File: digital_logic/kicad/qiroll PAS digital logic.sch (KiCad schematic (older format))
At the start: 21 parts, among them U1 14538, U2 4023, U3 4027, U4 14538, U5 L7805

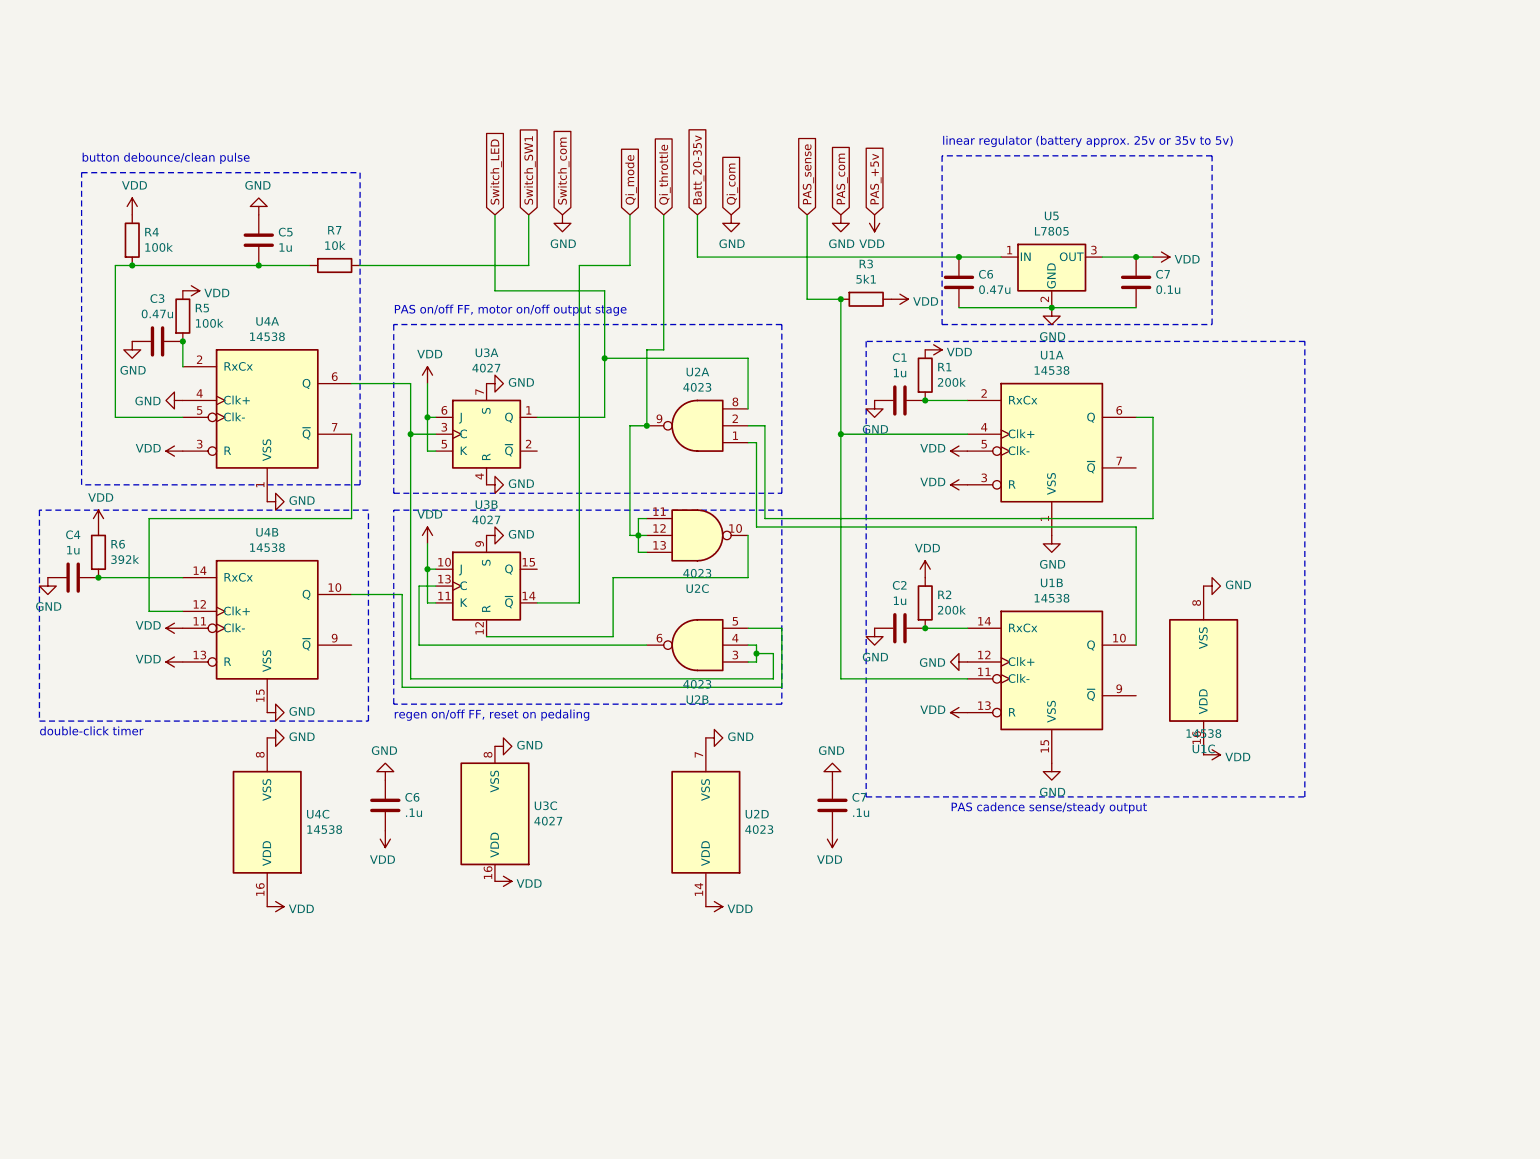
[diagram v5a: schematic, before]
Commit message: add electrolytic caps for stability
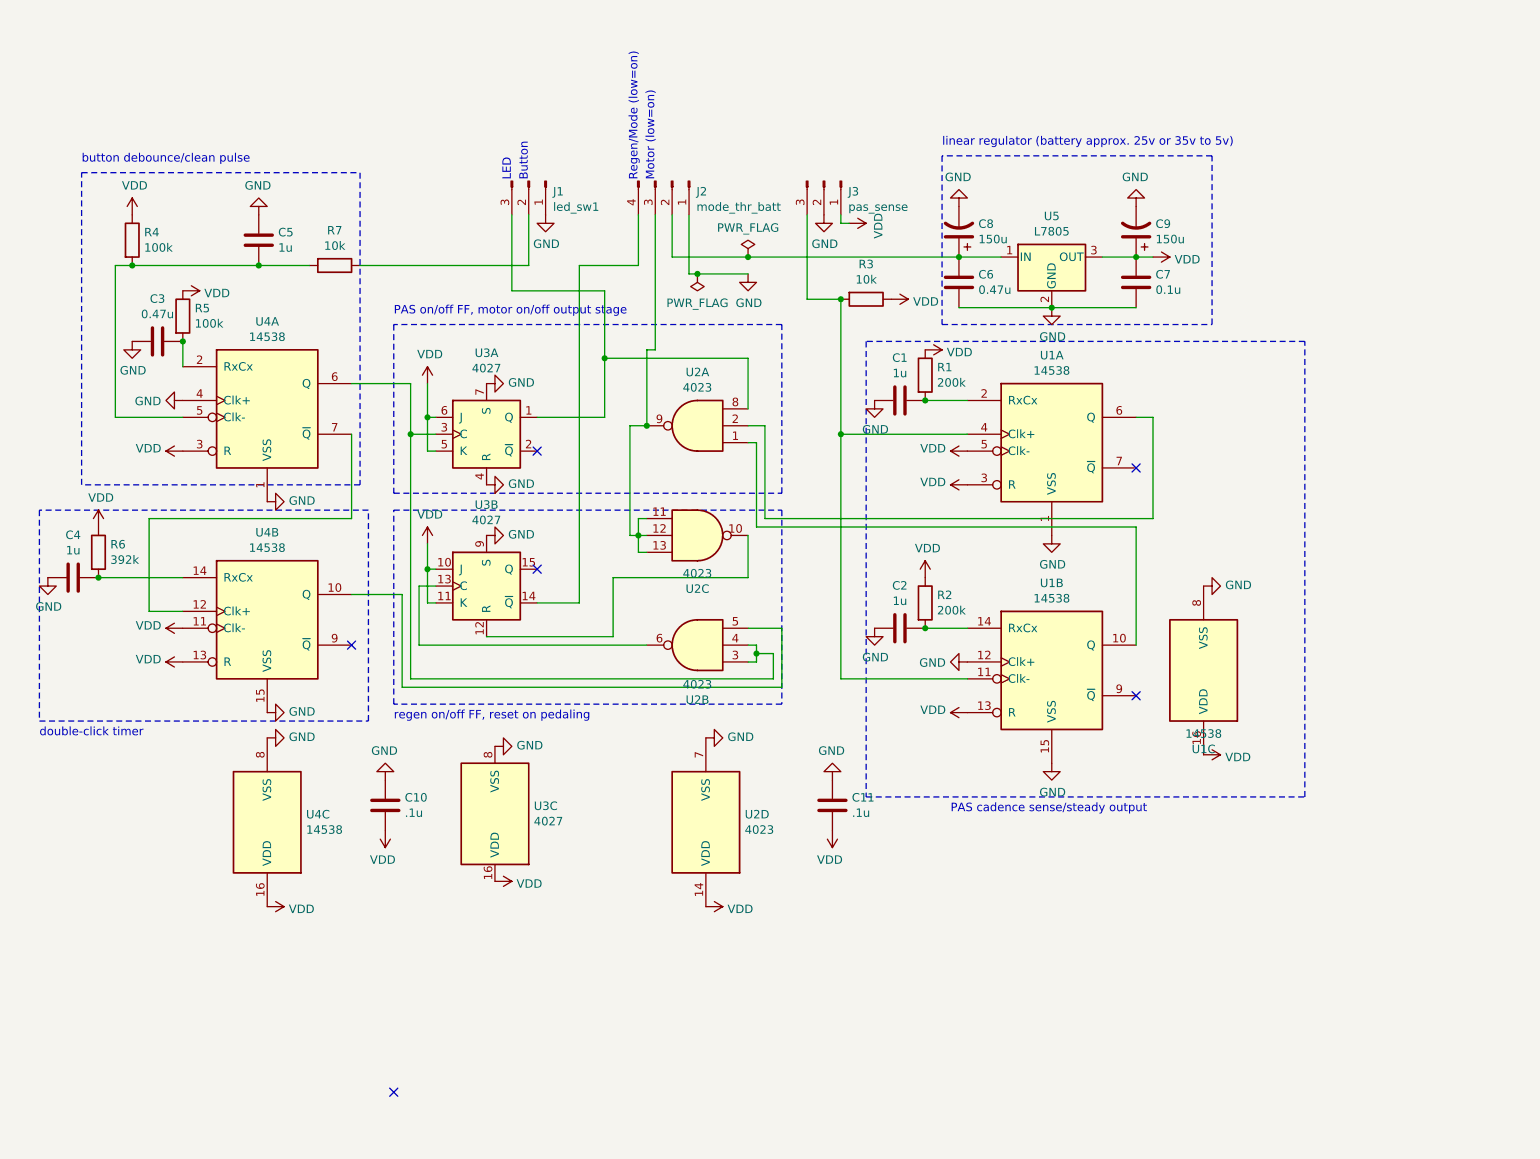
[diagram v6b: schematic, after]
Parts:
- added C8: 150u, Capacitor_THT:CP_Radial_D10.0mm_P5.00mm, symbol Device:CP1
- added C9: 150u, Capacitor_THT:CP_Radial_D5.0mm_P2.00mm, symbol Device:CP1
- added J1: led_sw1, Connector_PinHeader_2.54mm:PinHeader_1x03_P2.54mm_Vertical, symbol Connector:Conn_01x03_Male
- added J2: mode_thr_batt, Connector_Molex:Molex_KK-254_AE-6410-04A_1x04_P2.54mm_Vertical, symbol Connector:Conn_01x04_Male
- added J3: pas_sense, Connector_Molex:Molex_KK-254_AE-6410-03A_1x03_P2.54mm_Vertical, symbol Connector:Conn_01x03_Male
- C1, C2, C6, C7: footprint (none) -> Capacitor_SMD:C_0603_1608Metric
- C10: renamed from C6; footprint (none) -> Capacitor_SMD:C_0603_1608Metric
- C11: renamed from C7; footprint (none) -> Capacitor_SMD:C_0603_1608Metric
- C3, C4, C5: footprint (none) -> Capacitor_SMD:C_0201_0603Metric
- R1, R2, R4, R5, R6, R7: footprint (none) -> Resistor_SMD:R_0603_1608Metric
- R3: value 5k1 -> 10k; footprint (none) -> Resistor_SMD:R_0603_1608Metric
- U1, U3, U4: footprint (none) -> Package_SO:TSSOP-16_4.4x5mm_P0.65mm
- U2: footprint (none) -> Package_SO:TSSOP-14_4.4x5mm_P0.65mm
- U5: footprint (none) -> Package_TO_SOT_THT:TO-92
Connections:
- net GND: now also C8.2, C9.2, J1.1 (Pin_1), J2.1 (Pin_1), J3.2 (Pin_2)
- net VDD: now also C9.1, J3.1 (Pin_1)
- net Batt_20-35v: no longer names the net of C6.1, U5.1 (IN)
- net Batt_20-35v: now also C8.1, J2.2 (Pin_2)
- net PAS_sense: no longer names the net of R3.2, U1.11 (Clk-), U1.4 (Clk+)
- net PAS_sense: now also J3.3 (Pin_3)
- net Qi_mode: no longer names the net of U3.14 (~Q)
- net Qi_mode: now also J2.4 (Pin_4)
- net Qi_throttle: no longer names the net of U2.11, U2.12, U2.13, U2.9
- net Qi_throttle: now also J2.3 (Pin_3)
- net Switch_LED: no longer names the net of U2.8, U3.1 (Q)
- net Switch_LED: now also J1.3 (Pin_3)
- net Switch_SW1: no longer names the net of R7.1
- net Switch_SW1: now also J1.2 (Pin_2)
- no-connect marks 0 -> 6
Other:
- note added: "Button"
- note added: "LED"
- note added: "Motor (low=on)"
- note added: "Regen/Mode (low=on)"

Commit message: add voltage reg caps to schematic.png, start work on v2
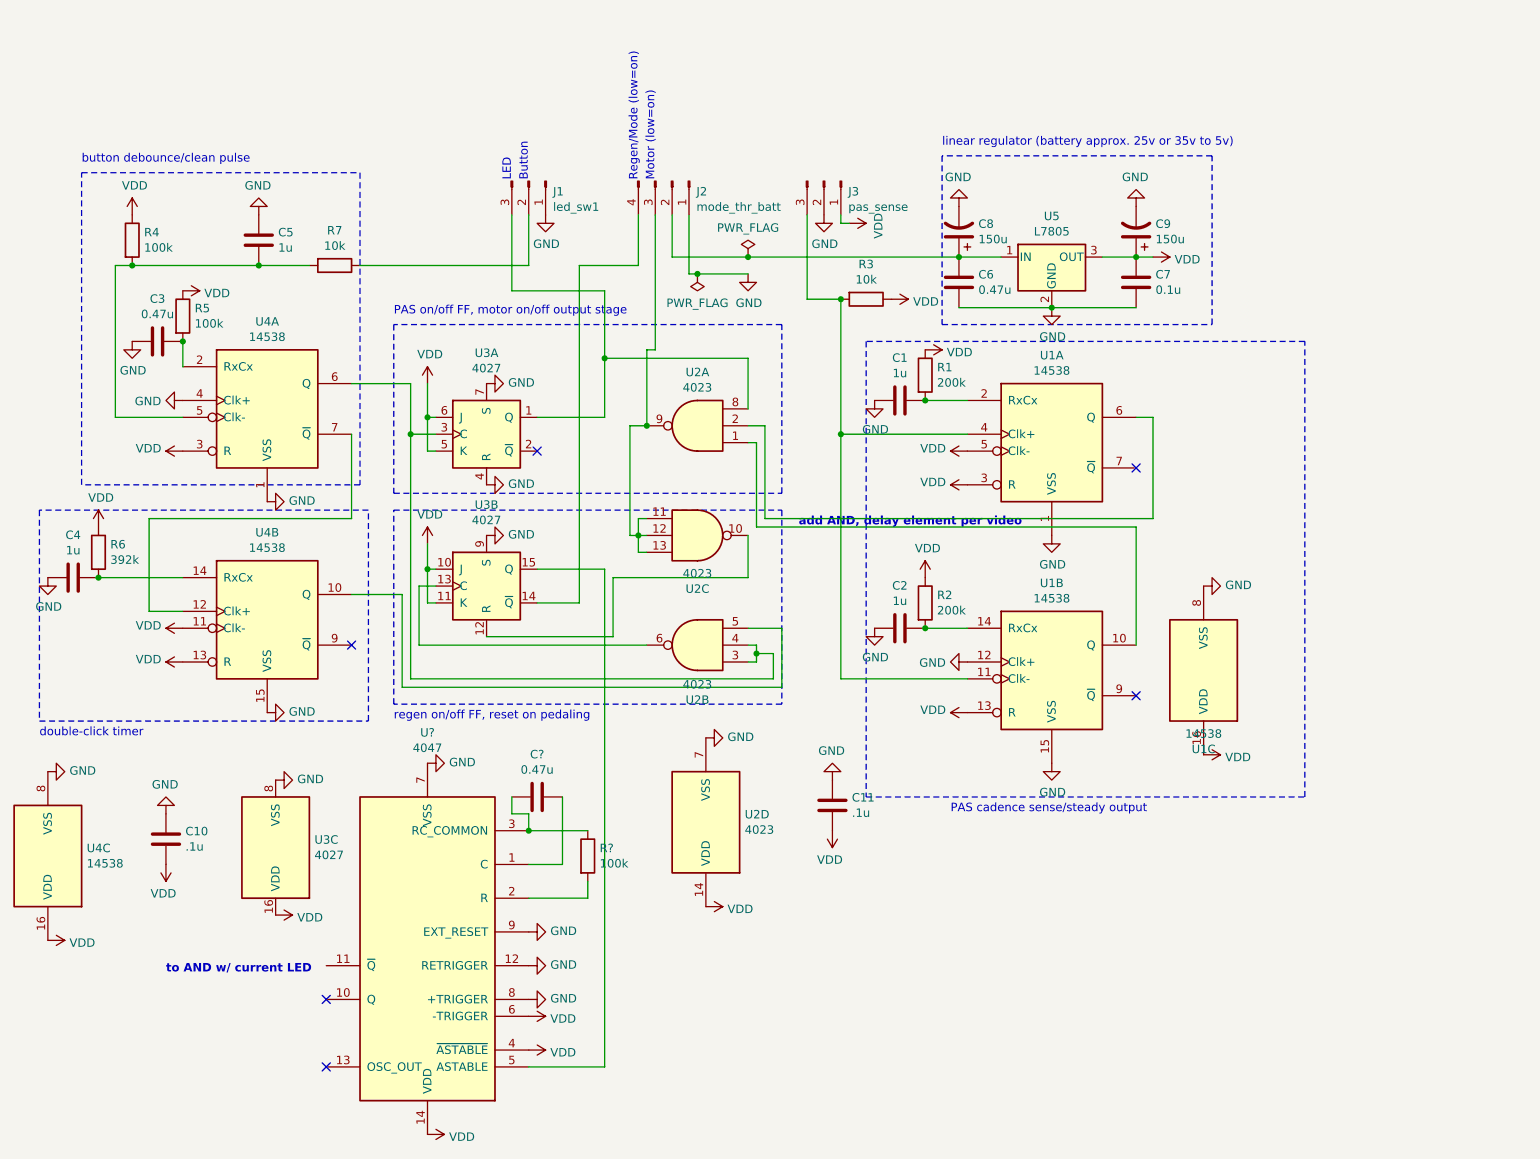
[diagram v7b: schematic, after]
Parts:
- added C?: 0.47u, symbol Device:C
- added R?: 100k, symbol Device:R
- added U?: 4047, symbol 4xxx:4047
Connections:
- net GND: now also U?.12 (RETRIGGER), U?.7 (VSS), U?.8 (+TRIGGER), U?.9 (EXT_RESET)
- net VDD: now also U?.14 (VDD), U?.4 (~ASTABLE), U?.6 (-TRIGGER)
- net at U3.15 (Q): now also U?.5 (ASTABLE)
- new net: C?.1, U?.1 (C)
- new net: R?.2, U?.2 (R)
- new net: C?.2, R?.1, U?.3 (RC_COMMON)
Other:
- note added: "add AND, delay element per video\n"
- note added: "to AND w/ current LED\n"
- moved on the sheet: C10, U3C, U4C

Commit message: pcb version 1, new features
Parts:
- added C11: 1u, Capacitor_SMD:C_0603_1608Metric, symbol Device:C
- added H1, H2, H3, H4: MountingHole_Pad, MountingHole:MountingHole_2.2mm_M2_DIN965_Pad, symbol Mechanical:MountingHole_Pad
- added J4: brk_sense, Connector_PinHeader_2.54mm:PinHeader_1x02_P2.54mm_Vertical, symbol Connector:Conn_01x02_Male
- added J5: jumper, Connector_PinHeader_2.54mm:PinHeader_2x02_P2.54mm_Vertical, symbol Connector_Generic:Conn_02x02_Odd_Even
- added R10: 1.6k, Resistor_SMD:R_0603_1608Metric, symbol Device:R
- added R9: 392K, Resistor_SMD:R_0603_1608Metric, symbol Device:R
- added U6: 4081, Package_SO:SOIC-14_3.9x8.7mm_P1.27mm, symbol 4xxx:4081
- added U8: 74VHC1G32, Package_SO:TSOP-5_1.65x3.05mm_P0.95mm, symbol 74xGxx:74AHC1G32
- C10: renamed from C?; footprint (none) -> Capacitor_SMD:C_0603_1608Metric
- C3, C4, C5: footprint Capacitor_SMD:C_0201_0603Metric -> Capacitor_SMD:C_0603_1608Metric
- C7: value 0.1u -> .1u
- C9: value 150u -> 200u; footprint Capacitor_THT:CP_Radial_D5.0mm_P2.00mm -> Capacitor_THT:CP_Radial_D6.3mm_P2.50mm
- J2: footprint Connector_Molex:Molex_KK-254_AE-6410-04A_1x04_P2.54mm_Vertical -> Connector_PinHeader_2.54mm:PinHeader_1x04_P2.54mm_Vertical
- J3: footprint Connector_Molex:Molex_KK-254_AE-6410-03A_1x03_P2.54mm_Vertical -> Connector_PinHeader_2.54mm:PinHeader_1x03_P2.54mm_Vertical
- R8: renamed from R?; footprint (none) -> Resistor_SMD:R_0603_1608Metric
- U1, U3, U4: footprint Package_SO:TSSOP-16_4.4x5mm_P0.65mm -> Package_SO:SOIC-16_3.9x9.9mm_P1.27mm
- U2: footprint Package_SO:TSSOP-14_4.4x5mm_P0.65mm -> Package_SO:SOIC-14_3.9x8.7mm_P1.27mm
- U7: renamed from U?; footprint (none) -> Package_SO:SOIC-14_3.9x8.7mm_P1.27mm
- renumbered C10 to C12, C11 to C13
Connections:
- net GND: now also C11.1, H1.1, H2.1, H3.1, H4.1, U6.7 (VSS), U8.3 (GND); no longer U3.9 (S)
- net at U1.6 (Q): now also U6.8; no longer U2.2
- net at U1.10 (Q): now also U6.9; no longer U2.1
- net PAS_ON: now reaches U2.8, U3.1 (Q)
- net PAS_ON: now also U6.1; no longer J1.3 (Pin_3)
- net PAS_OFF: now reaches U3.2 (~Q)
- net PAS_OFF: now also U6.12
- net at U2.10: now also U2.1, U6.6; no longer U3.12 (R)
- net at U2.6, U3.13 (C): now also J5.2 (Pin_2)
- net at U3.14 (~Q): now also J5.4 (Pin_4); no longer J2.4 (Pin_4)
- net BRK: now reaches U2.11, U2.12, U2.13
- net BRK: now also U3.9 (S), J4.1 (Pin_1); no longer J2.3 (Pin_3), U2.9
- net at C6.1, C8.1, U5.1 (IN): now also R10.1; no longer J2.2 (Pin_2)
- net at U7.10 (Q): now also U6.13
- net RGN_FLSH: now reaches U7.11 (~Q)
- net RGN_FLSH: now also U6.2
- net VDD renamed VCC
- net VCC: now also J4.2 (Pin_2), U6.14 (VDD), U8.5 (VCC)
- new net: R9.2, U2.9
- new net: J1.3 (Pin_3), U8.4
- new net: J2.2 (Pin_2), R10.2
- new net: J2.3 (Pin_3), U6.4
- new net: J2.4 (Pin_4), J5.1 (Pin_1), J5.3 (Pin_3)
- new net: U6.3, U8.2
- new net: C11.2, R9.1, U6.5
- new net PEDAL: U2.2, U3.12 (R), U6.10
- new net RGN_FLSH_2: U6.11, U8.1
- no-connect marks 6 -> 4
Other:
- note added: "*"
- note added: "PTH for \nbodge!"
- note removed: "add AND, delay element per video\n"
- note removed: "to AND w/ current LED\n"
- moved on the sheet: C13
